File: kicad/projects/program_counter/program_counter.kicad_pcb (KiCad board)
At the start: 2 copper layers, 203.2 x 97.8 mm, 43 parts, among them J1 Conn_01x16_Female, J2 Control_signal_backplane, J3 Bus_connection, J4 Aux_connection, U1 74HC04, U2 74HC245, U3 74HC161, U4 74HC245, U5 74HC161, U6 74HC245, U7 74HC161, U8 74HC245, U9 74HC161

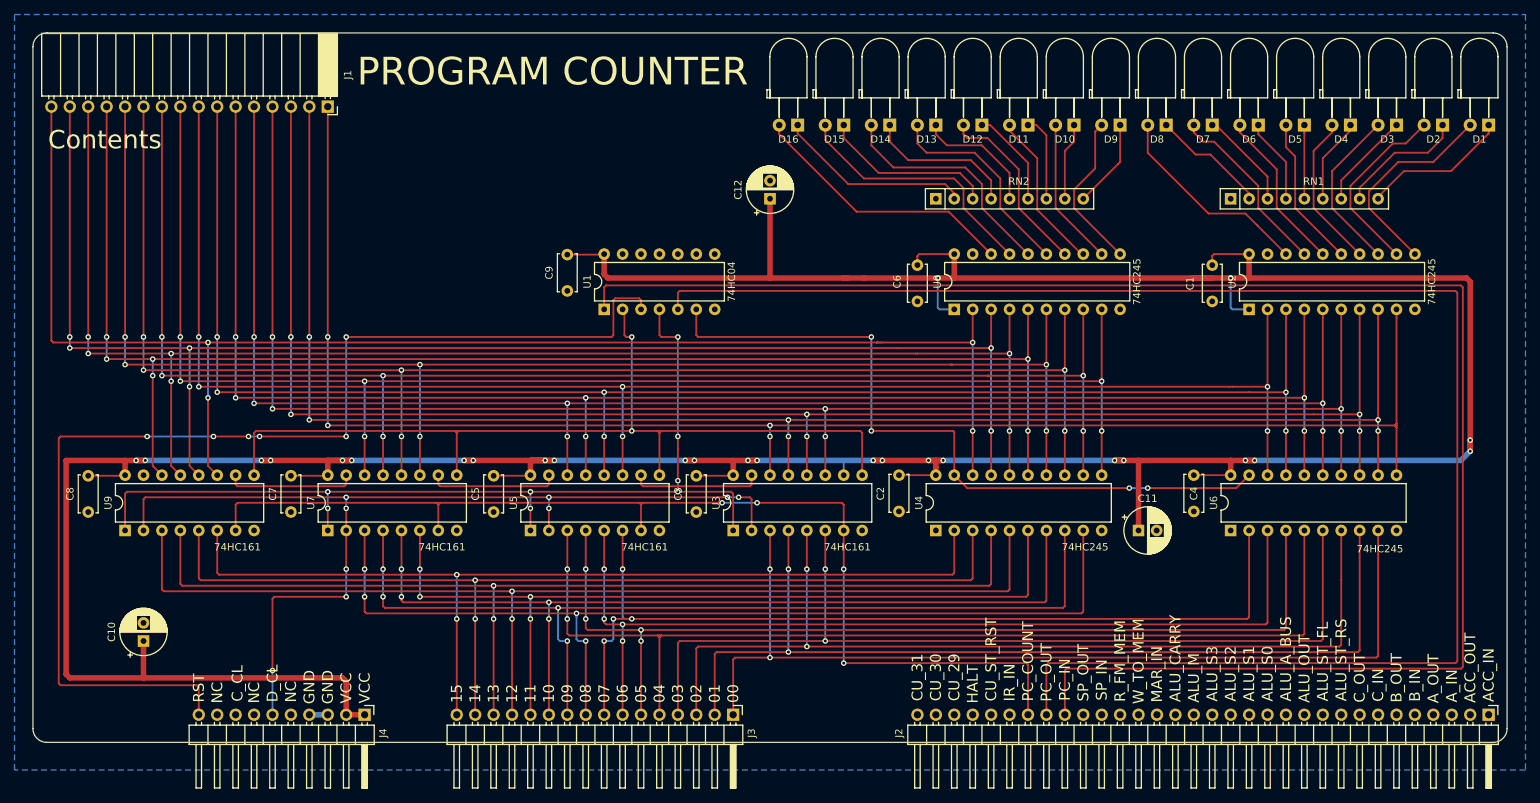
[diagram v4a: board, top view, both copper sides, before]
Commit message: Adjust lower connector position on program counter.
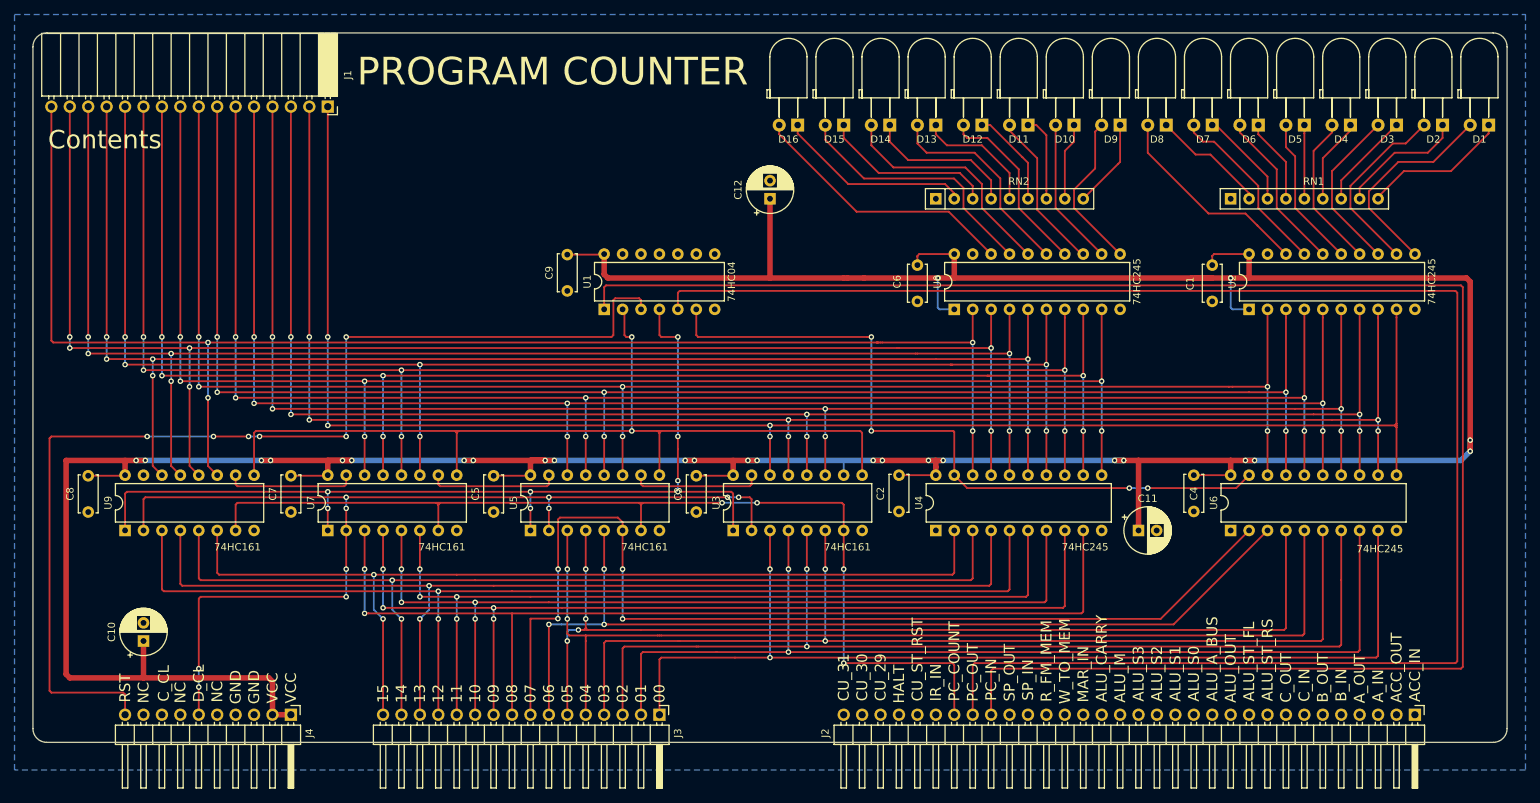
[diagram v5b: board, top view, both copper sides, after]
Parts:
- moved J2 10.2 mm to (241.3, 144.8)
- moved J3 10.2 mm to (137.2, 144.8)
- moved J4 10.2 mm to (86.4, 144.8)
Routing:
- net /BUS_07: track 127.3 -> 144.7 mm
- net VCC: track 551.5 -> 541.3 mm
- net /PC_IN: track 235.1 -> 245.3 mm
- net /PC_COUNT: track 150.9 -> 140.7 mm
- net /PC_OUT: track 224.4 -> 234.6 mm
- net /DATA_CLK: track 137.2 -> 147.4 mm, vias 9 -> 10
- net /BUS_02: track 130.0 -> 140.2 mm
- net /BUS_00: track 131.5 -> 141.7 mm
- net /BUS_03: track 129.2 -> 139.4 mm
- net /BUS_01: track 130.8 -> 140.9 mm
- net /RESET: track 157.6 -> 150.0 mm
- net /BUS_05: track 135.3 -> 138.3 mm
- net GND: track 2.54 -> 0.00 mm
- net /BUS_09: track 130.9 -> 129.9 mm
- net /BUS_08: track 136.7 -> 135.7 mm, vias 4 -> 2
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
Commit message: Add top power and LED control to program counter.
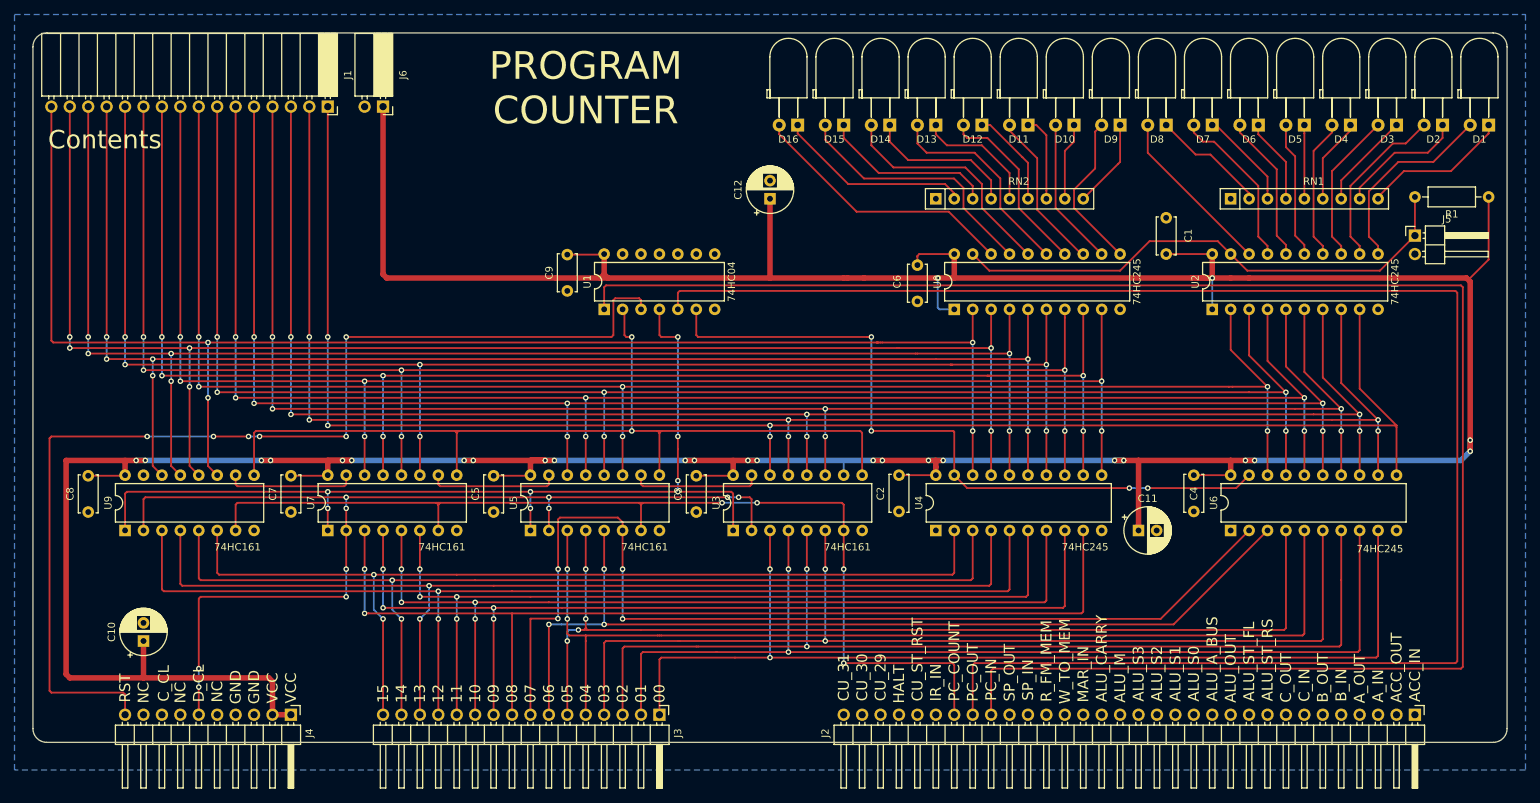
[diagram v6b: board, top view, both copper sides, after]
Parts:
- added J5: LED_CONTROL, Connector_PinHeader_2.54mm:PinHeader_1x02_P2.54mm_Horizontal, F.Cu at (241.3, 78.7)
- added J6: TOP_POWER, Connector_PinSocket_2.54mm:PinSocket_1x02_P2.54mm_Horizontal, F.Cu at (99.1, 61.0)
- added R1: 10K, Resistor_THT:R_Axial_DIN0207_L6.3mm_D2.5mm_P10.16mm_Horizontal, F.Cu at (251.5, 73.4)
- moved C1 6.53 mm to (207.0, 81.3), turned to 90 degrees
- moved U2 5.08 mm to (213.4, 88.9)
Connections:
- U2 pad 19: GND -> /LED_CONTROL
- U8 pad 19: GND -> /LED_CONTROL
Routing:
- net /LED_CONTROL: track 0.00 -> 72.6 mm
- net VCC: track 541.3 -> 606.1 mm
- net Net-(D8-Pad2): track 28.6 -> 23.6 mm
- net /CTNT_06: track 221.0 -> 223.1 mm
- net /CTNT_05: track 221.2 -> 223.3 mm
- net /CTNT_02: track 221.0 -> 223.1 mm
- net Net-(D1-Pad2): track 29.0 -> 26.9 mm
- net Net-(D7-Pad2): track 25.0 -> 22.9 mm
- net Net-(D4-Pad2): track 21.5 -> 19.4 mm
- net Net-(D3-Pad2): track 23.0 -> 20.9 mm
- net /CTNT_01: track 221.0 -> 223.1 mm
- net Net-(D6-Pad2): track 22.5 -> 20.4 mm
- net Net-(D5-Pad2): track 20.9 -> 18.8 mm
- net Net-(D2-Pad2): track 25.7 -> 23.6 mm
- net /CTNT_07: track 221.0 -> 223.1 mm
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
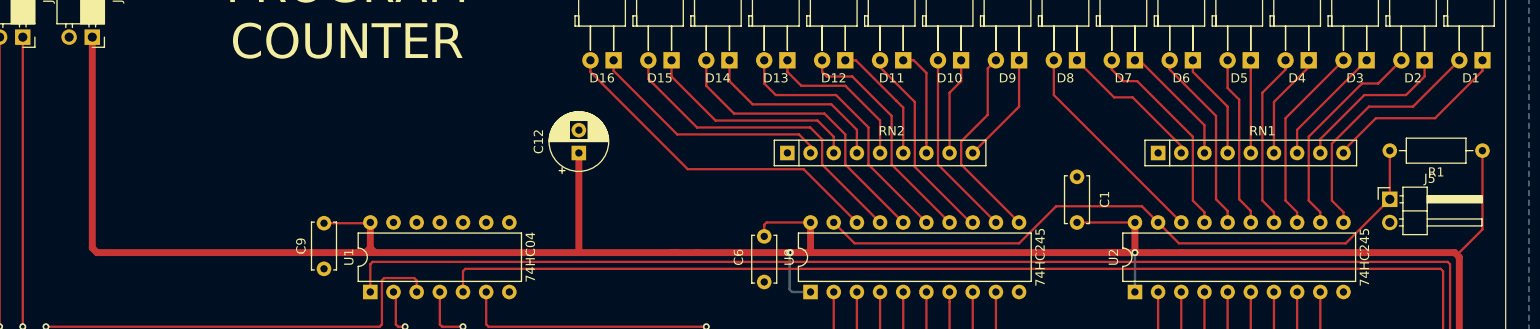
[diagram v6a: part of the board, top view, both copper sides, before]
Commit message: Better labels on ALU. Top power and LED control on register.
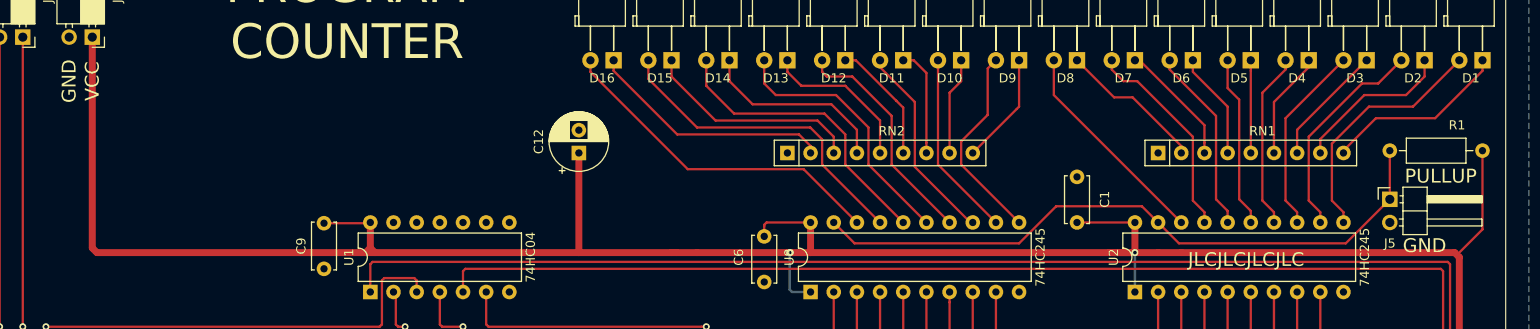
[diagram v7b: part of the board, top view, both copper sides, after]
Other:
- board text added: "GND"
- board text added: "JLCJLCJLCJLC"
- board text added: "PULLUP"
- board text added: "VCC"
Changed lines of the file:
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@@
   (general
     (thickness 1.6)
-    (drawings 10)
+    (drawings 15)
     (tracks 967)
     (zones 0)
@@
     (descr "Resistor, Axial_DIN0207 series, Axial, Horizontal, pin pitch=10.16mm, 0.25W = 1/4W, length*diameter=6.3*2.5mm^2, http://cdn-reichelt.de/documents/datenblatt/B400/1_4W%23YAG.pdf")
     (tags "Resistor Axial_DIN0207 series Axial Horizontal pin pitch 10.16mm 0.25W = 1/4W length 6.3mm diameter 2.5mm")
-    (fp_text reference R1 (at 5.08 -2.37) (layer F.SilkS)
+    (fp_text reference R1 (at 2.794 2.794) (layer F.SilkS)
       (effects (font (size 1 1) (thickness 0.15)))
     )
@@
     (descr "Through hole angled pin header, 1x02, 2.54mm pitch, 6mm pin length, single row")
     (tags "Through hole angled pin header THT 1x02 2.54mm single row")
-    (fp_text reference J5 (at 4.385 -2.27) (layer F.SilkS)
+    (fp_text reference J5 (at 0 4.826) (layer F.SilkS)
       (effects (font (size 1 1) (thickness 0.15)))
     )
@@
     )
   )
+  (gr_text JLCJLCJLCJLC (at 225.552 85.344) (layer F.SilkS)
+    (effects (font (size 1.5 1.5) (thickness 0.3)))
+  )
+  (gr_text GND (at 245.11 83.82) (layer F.SilkS)
+    (effects (font (size 1.524 1.524) (thickness 0.254)))
+  )
+  (gr_text PULLUP (at 246.888 76.2) (layer F.SilkS)
+    (effects (font (size 1.524 1.524) (thickness 0.254)))
+  )
+  (gr_text GND (at 96.52 65.786 90) (layer F.SilkS)
+    (effects (font (size 1.524 1.524) (thickness 0.254)))
+  )
+  (gr_text VCC (at 99.06 65.786 90) (layer F.SilkS)
+    (effects (font (size 1.524 1.524) (thickness 0.254)))
+  )
   (gr_text Contents (at 60.706 65.532) (layer F.SilkS)

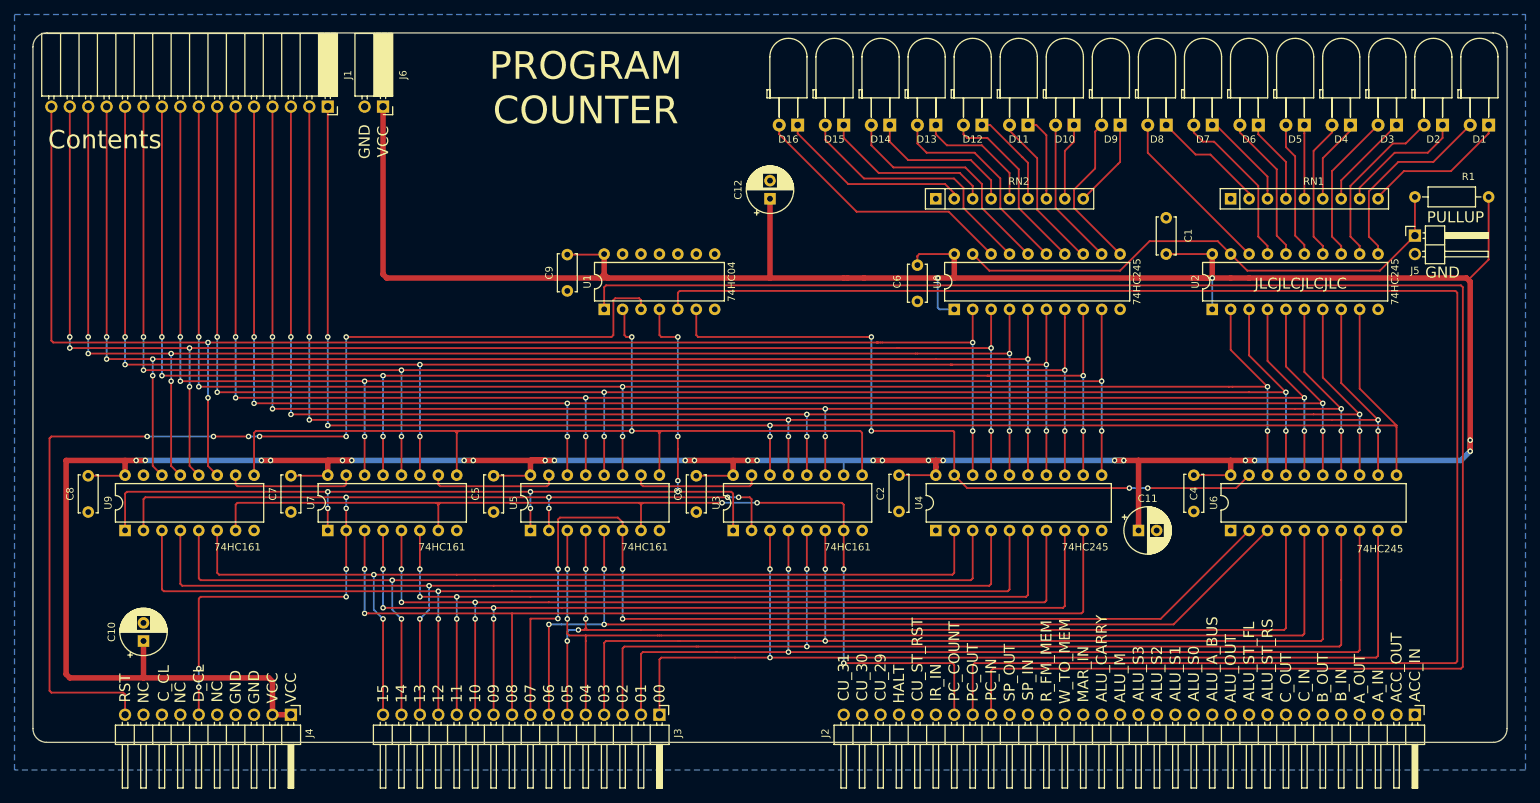
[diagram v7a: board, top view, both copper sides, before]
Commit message: Add pullup on bus out on program counter and update LED control.
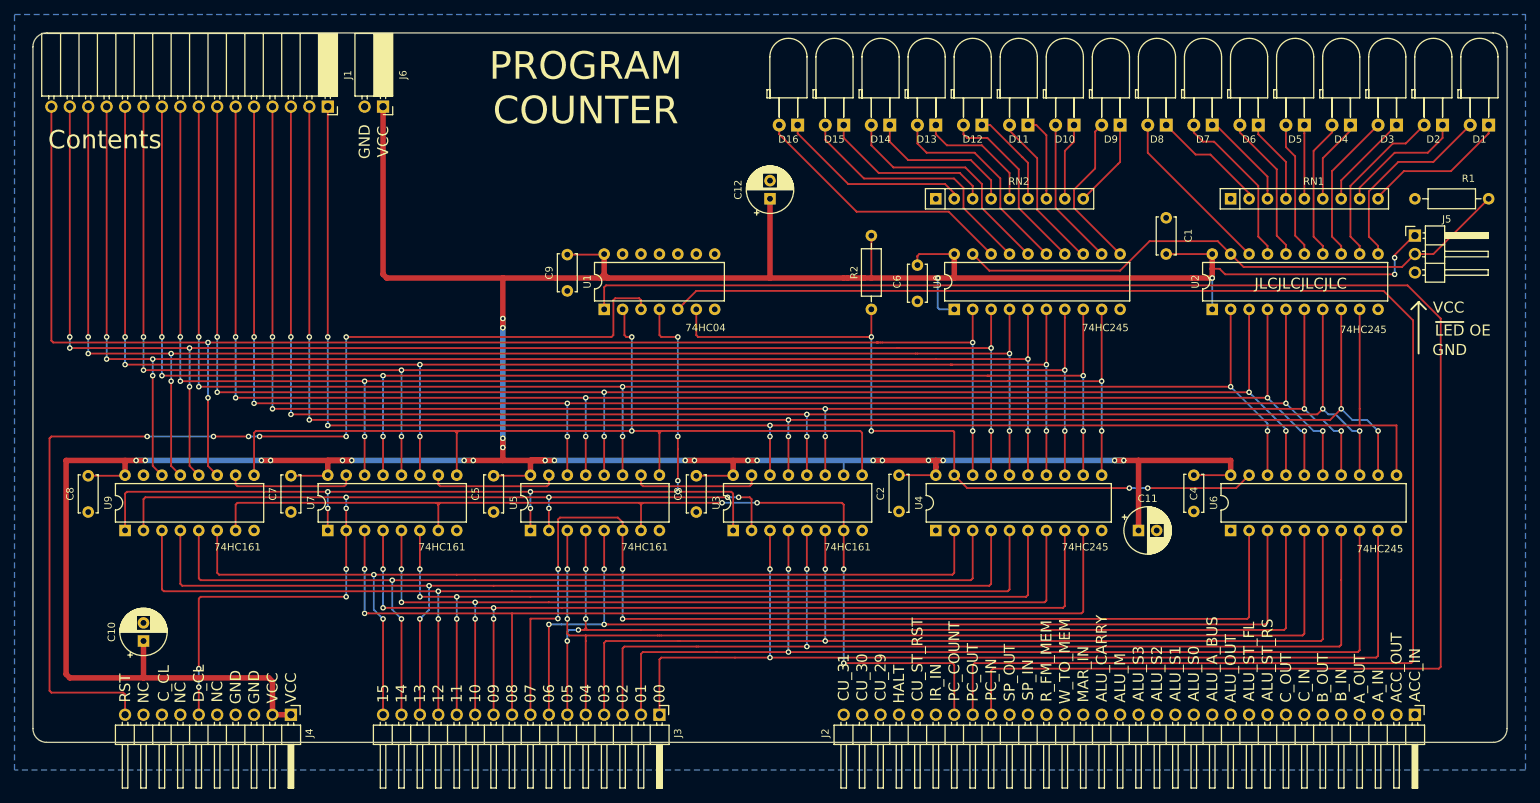
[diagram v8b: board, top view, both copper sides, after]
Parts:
- added R2: 10K, Resistor_THT:R_Axial_DIN0207_L6.3mm_D2.5mm_P10.16mm_Horizontal, F.Cu at (166.4, 88.9)
- J5: footprint Connector_PinHeader_2.54mm:PinHeader_1x02_P2.54mm_Horizontal -> Connector_PinHeader_2.54mm:PinHeader_1x03_P2.54mm_Horizontal
- moved R1 0.25 mm to (251.5, 73.7)
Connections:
- J5 pad 1: /LED_CONTROL -> VCC
- J5 pad 2: GND -> /LED_CONTROL
- R1 pad 1: VCC -> /LED_CONTROL
- R1 pad 2: /LED_CONTROL -> GND
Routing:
- net VCC: track 606.1 -> 561.6 mm, vias 26 -> 28
- net /PC_OUT: track 234.6 -> 218.8 mm
- net /PC_IN: track 245.3 -> 236.7 mm
- net /BUS_06: track 129.8 -> 137.3 mm
- net /BUS_07: track 144.7 -> 151.7 mm
- net /LED_CONTROL: track 72.6 -> 79.1 mm
- net /CTNT_07: track 223.1 -> 218.0 mm
- net /CTNT_06: track 223.1 -> 218.0 mm
- net /CTNT_05: track 223.3 -> 218.6 mm
- net /CTNT_04: track 223.1 -> 218.7 mm
- net /CTNT_03: track 223.1 -> 219.2 mm
- net /~PC_OUT: track 100.3 -> 104.1 mm
- net /CTNT_02: track 223.1 -> 219.5 mm
- net /CTNT_01: track 223.1 -> 219.8 mm
- net /CTNT_00: track 223.1 -> 221.0 mm
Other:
- board text added: "~LED OE"
- board text removed: "PULLUP"
